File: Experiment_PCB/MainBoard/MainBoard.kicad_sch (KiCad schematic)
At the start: 43 parts, among them U1 Teensy4.1

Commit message: Incorporate feedback
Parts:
- removed R10, R11, R12, R13, R14, R15, R16, R17, R18, R19, R2, R20, R21, R22, R23, R24, R25, R26, R27, R28, R29, R3, R30, R31, R32, R33, R34, R35, R36, R4, R5, R6, R7, R8, R9: 10k, Resistor_SMD:R_0402_1005Metric, symbol Device:R
- added C1, C2, C3: 10u, Capacitor_SMD:C_0603_1608Metric, symbol Device:C
- R1: value 10k -> 10
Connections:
- net CS1: now also master_connector_input1.9 (CS1); no longer master_connector_input1.10 (CS1)
- net CS10: now also master_connector_input2.12 (CS4); no longer master_connector_input2.13 (CS4)
- net CS11: now also master_connector_input2.13 (CS5); no longer master_connector_input2.14 (CS5)
- net CS12: now also master_connector_input2.14 (CS6); no longer master_connector_input2.15 (CS6)
- net CS13: now also master_connector_input3.9 (CS1); no longer master_connector_input3.10 (CS1)
- net CS14: now also master_connector_input3.10 (CS2); no longer master_connector_input3.11 (CS2)
- net CS15: now also master_connector_input3.11 (CS3); no longer master_connector_input3.12 (CS3)
- net CS16: now also master_connector_input3.12 (CS4); no longer master_connector_input3.13 (CS4)
- net CS17: now also master_connector_input3.13 (CS5); no longer master_connector_input3.14 (CS5)
- net CS18: now also master_connector_input3.14 (CS6); no longer master_connector_input3.15 (CS6)
- net CS19: now also master_connector_input6.9 (CS1); no longer master_connector_input6.10 (CS1)
- net CS2: now also master_connector_input1.10 (CS2); no longer master_connector_input1.11 (CS2)
- net CS20: now also master_connector_input6.10 (CS2); no longer master_connector_input6.11 (CS2)
- net CS21: now also master_connector_input6.11 (CS3); no longer master_connector_input6.12 (CS3)
- net CS22: now also master_connector_input6.12 (CS4); no longer master_connector_input6.13 (CS4)
- net CS23: now also master_connector_input6.13 (CS5); no longer master_connector_input6.14 (CS5)
- net CS24: now also master_connector_input6.14 (CS6); no longer master_connector_input6.15 (CS6)
- net CS25: now also master_connector_input5.9 (CS1); no longer master_connector_input5.10 (CS1)
- net CS26: now also master_connector_input5.10 (CS2); no longer master_connector_input5.11 (CS2)
- net CS27: now also master_connector_input5.11 (CS3); no longer master_connector_input5.12 (CS3)
- net CS28: now also master_connector_input5.12 (CS4); no longer master_connector_input5.13 (CS4)
- net CS29: now also master_connector_input5.13 (CS5); no longer master_connector_input5.14 (CS5)
- net CS3: now also master_connector_input1.11 (CS3); no longer master_connector_input1.12 (CS3)
- net CS30: now also master_connector_input5.14 (CS6); no longer master_connector_input5.15 (CS6)
- net CS31: now also master_connector_input4.9 (CS1); no longer master_connector_input4.10 (CS1)
- net CS32: now also master_connector_input4.10 (CS2); no longer master_connector_input4.11 (CS2)
- net CS33: now also master_connector_input4.11 (CS3); no longer master_connector_input4.12 (CS3)
- net CS34: now also master_connector_input4.12 (CS4); no longer master_connector_input4.13 (CS4)
- net CS35: now also master_connector_input4.13 (CS5); no longer master_connector_input4.14 (CS5)
- net CS36: now also master_connector_input4.14 (CS6); no longer master_connector_input4.15 (CS6)
- net CS4: now also master_connector_input1.12 (CS4); no longer master_connector_input1.13 (CS4)
- net CS5: now also master_connector_input1.13 (CS5); no longer master_connector_input1.14 (CS5)
- net CS6: now also master_connector_input1.14 (CS6); no longer master_connector_input1.15 (CS6)
- net CS7: now also master_connector_input2.9 (CS1); no longer R1.1, master_connector_input2.10 (CS1)
- net CS8: now also master_connector_input2.10 (CS2); no longer master_connector_input2.11 (CS2)
- net CS9: now also master_connector_input2.11 (CS3); no longer master_connector_input2.12 (CS3)
- net GND: now also C1.1, C2.1, C3.1
- net MISO: now also master_connector_input1.4 (MISO), master_connector_input2.4 (MISO), master_connector_input3.4 (MISO), master_connector_input4.4 (MISO), master_connector_input5.4 (MISO), master_connector_input6.4 (MISO); no longer master_connector_input1.5 (MISO), master_connector_input2.5 (MISO), master_connector_input3.5 (MISO), master_connector_input4.5 (MISO), master_connector_input5.5 (MISO), master_connector_input6.5 (MISO)
- net MISO1: now also master_connector_input1.7 (MISO1), master_connector_input2.7 (MISO1), master_connector_input3.7 (MISO1), master_connector_input4.7 (MISO1), master_connector_input5.7 (MISO1), master_connector_input6.7 (MISO1); no longer master_connector_input1.8 (MISO1), master_connector_input2.8 (MISO1), master_connector_input3.8 (MISO1), master_connector_input4.8 (MISO1), master_connector_input5.8 (MISO1), master_connector_input6.8 (MISO1)
- net MOSI: now also master_connector_input1.5 (MOSI), master_connector_input2.5 (MOSI), master_connector_input3.5 (MOSI), master_connector_input4.5 (MOSI), master_connector_input5.5 (MOSI), master_connector_input6.5 (MOSI); no longer master_connector_input1.6 (MOSI), master_connector_input2.6 (MOSI), master_connector_input3.6 (MOSI), master_connector_input4.6 (MOSI), master_connector_input5.6 (MOSI), master_connector_input6.6 (MOSI)
- net MOSI1: now also master_connector_input1.8 (MOSI1), master_connector_input2.8 (MOSI1), master_connector_input3.8 (MOSI1), master_connector_input4.8 (MOSI1), master_connector_input5.8 (MOSI1), master_connector_input6.8 (MOSI1); no longer master_connector_input1.9 (MOSI1), master_connector_input2.9 (MOSI1), master_connector_input3.9 (MOSI1), master_connector_input4.9 (MOSI1), master_connector_input5.9 (MOSI1), master_connector_input6.9 (MOSI1)
- net SCK: now also master_connector_input1.3 (SCK), master_connector_input2.3 (SCK), master_connector_input3.3 (SCK), master_connector_input4.3 (SCK), master_connector_input5.3 (SCK), master_connector_input6.3 (SCK); no longer master_connector_input1.4 (SCK), master_connector_input2.4 (SCK), master_connector_input3.4 (SCK), master_connector_input4.4 (SCK), master_connector_input5.4 (SCK), master_connector_input6.4 (SCK)
- net SCK1: now also master_connector_input1.6 (SCK1), master_connector_input2.6 (SCK1), master_connector_input3.6 (SCK1), master_connector_input4.6 (SCK1), master_connector_input5.6 (SCK1), master_connector_input6.6 (SCK1); no longer master_connector_input1.7 (SCK1), master_connector_input2.7 (SCK1), master_connector_input3.7 (SCK1), master_connector_input4.7 (SCK1), master_connector_input5.7 (SCK1), master_connector_input6.7 (SCK1)
- net VDD: now also R1.1, master_connector_input1.1 (VDD), master_connector_input2.1 (VDD), master_connector_input3.1 (VDD), master_connector_input4.1 (VDD), master_connector_input5.1 (VDD), master_connector_input6.1 (VDD), C1.2, C2.2, C3.2; no longer R1.2, U1.15 (3V3), master_connector_input1.3 (VDD), master_connector_input2.3 (VDD), master_connector_input3.3 (VDD), master_connector_input4.3 (VDD), master_connector_input5.3 (VDD), master_connector_input6.3 (VDD)
- removed net VDDIO: U1.46 (3V3), master_connector_input1.1 (VDDIO), master_connector_input2.1 (VDDIO), master_connector_input3.1 (VDDIO), master_connector_input4.1 (VDDIO), master_connector_input5.1 (VDDIO), master_connector_input6.1 (VDDIO)
- new net 3.3V: R1.2, U1.46 (3V3)

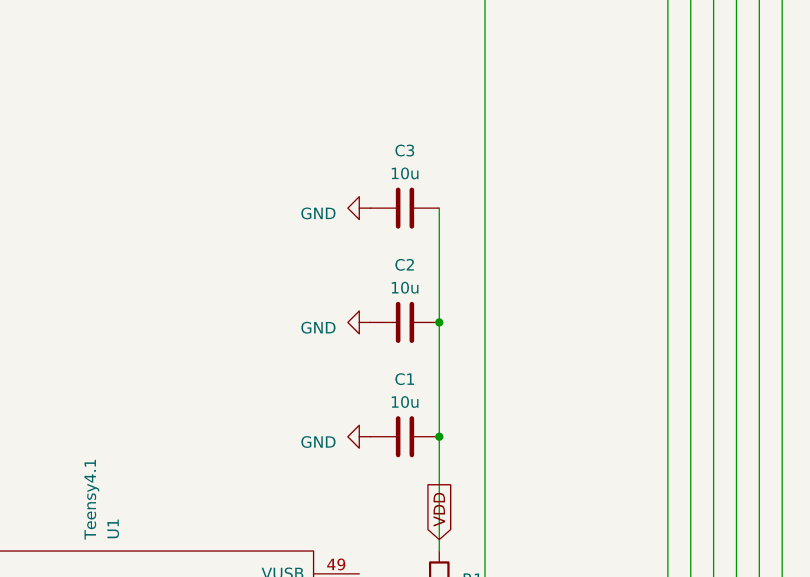
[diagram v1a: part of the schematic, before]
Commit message: update for file transfer / cleanup some traces
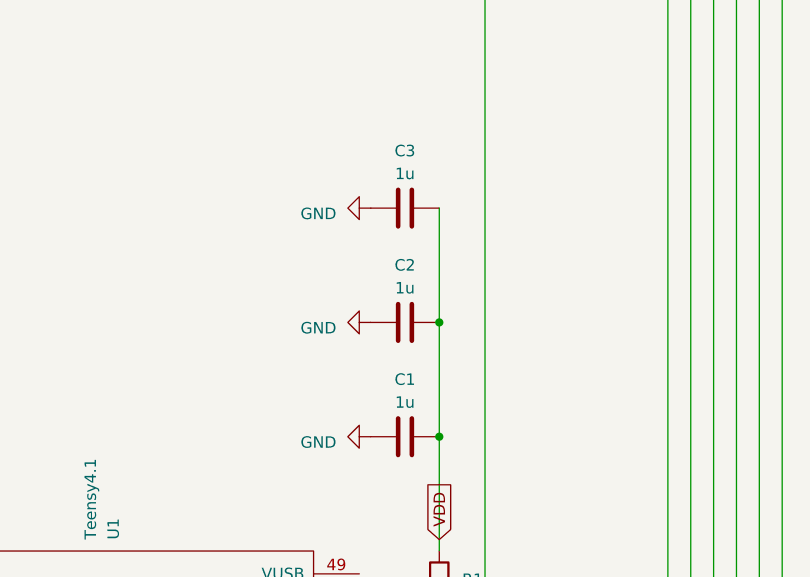
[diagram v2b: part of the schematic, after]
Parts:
- C1, C2, C3: value 10u -> 1u
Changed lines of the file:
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@@
       (effects (font (size 1.27 1.27)))
     )
-    (property "Value" "10u" (at 250.19 135.89 90)
+    (property "Value" "1u" (at 250.19 135.89 90)
       (effects (font (size 1.27 1.27)))
     )
@@
       (effects (font (size 1.27 1.27)))
     )
-    (property "Value" "10u" (at 250.19 123.19 90)
+    (property "Value" "1u" (at 250.19 123.19 90)
       (effects (font (size 1.27 1.27)))
     )
@@
       (effects (font (size 1.27 1.27)))
     )
-    (property "Value" "10u" (at 250.19 148.59 90)
+    (property "Value" "1u" (at 250.19 148.59 90)
       (effects (font (size 1.27 1.27)))
     )
